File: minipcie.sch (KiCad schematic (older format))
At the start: 1 part

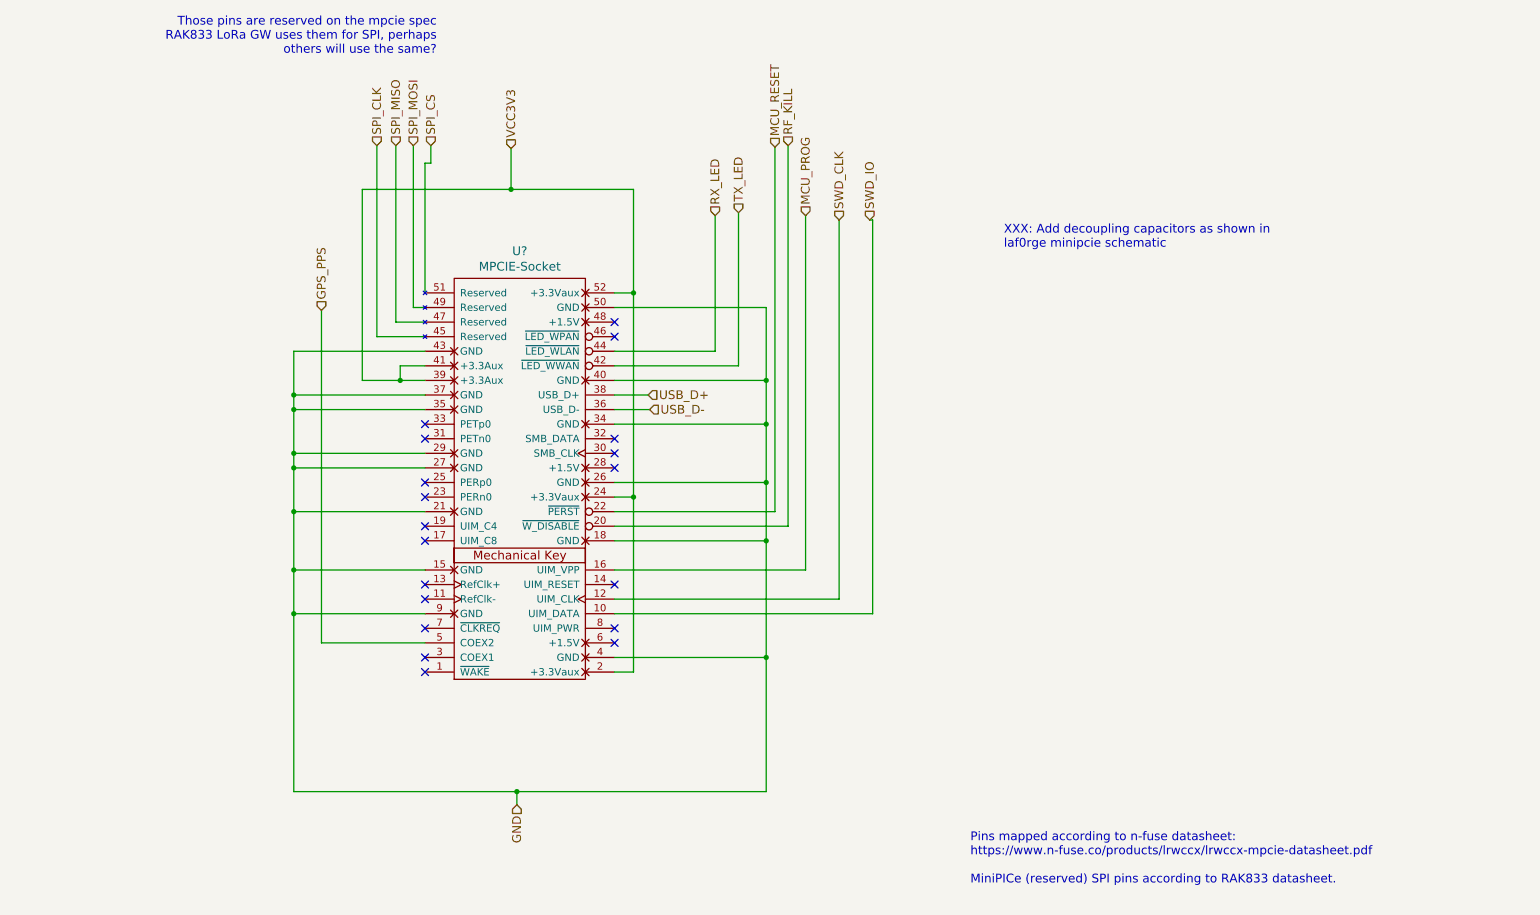
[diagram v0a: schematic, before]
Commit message: Add all POE logic with the si3404, schematic almost finished.
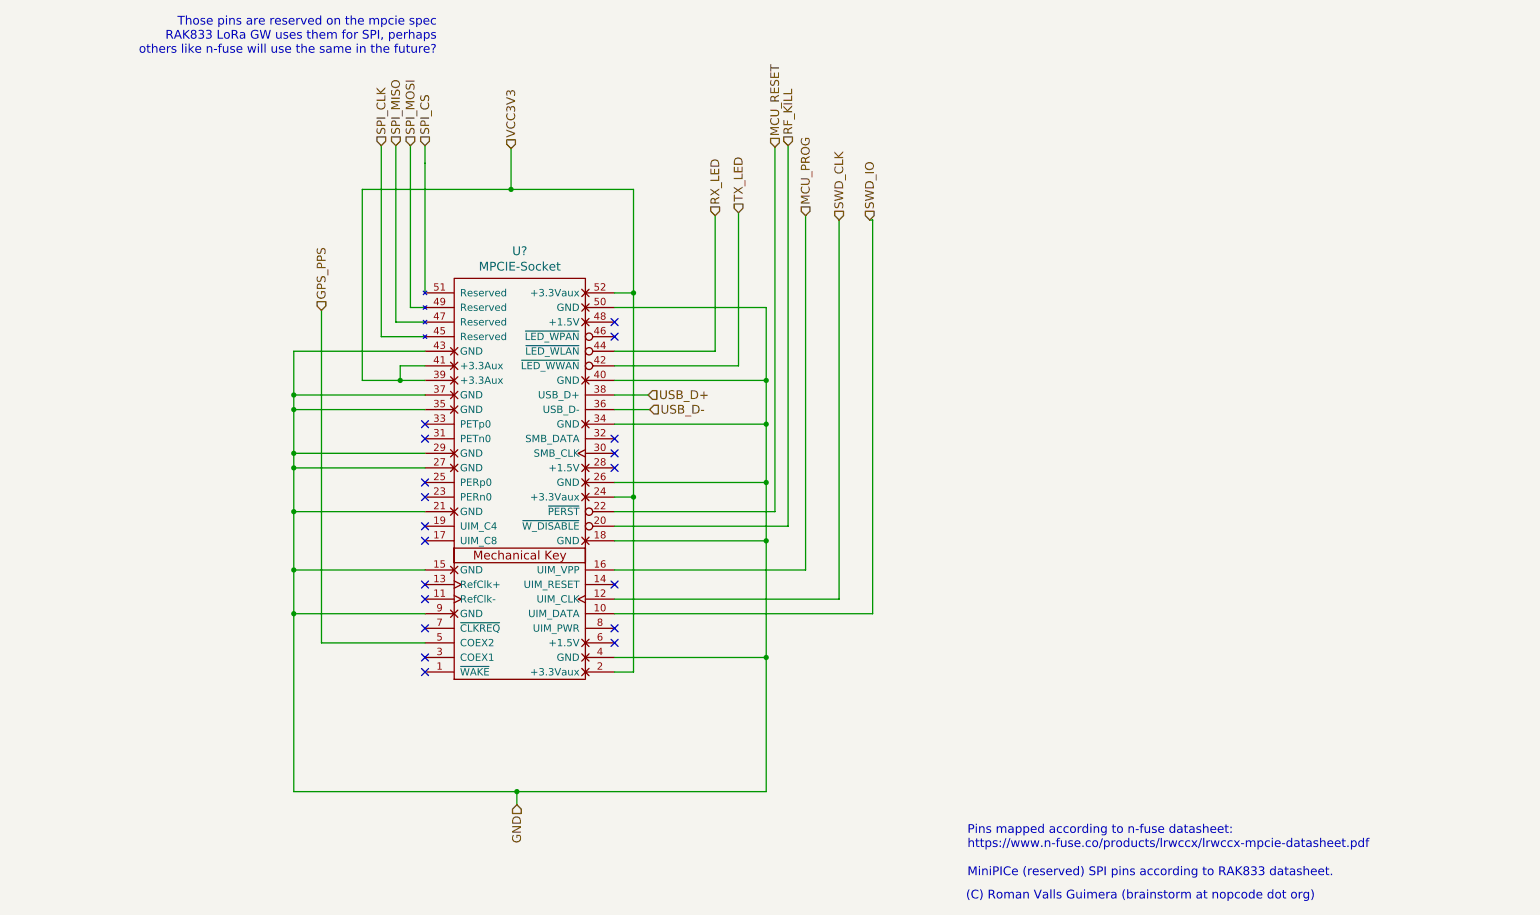
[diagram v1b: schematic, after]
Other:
- note added: "(C) Roman Valls Guimera (brainstorm at nopcode dot org)"
- note added: "Those pins are reserved on the mpcie spec\nRAK833 LoRa GW uses them for SPI, perhaps\nothers like n-fuse will use the same in the future?"
- note removed: "Those pins are reserved on the mpcie spec\nRAK833 LoRa GW uses them for SPI, perhaps\nothers will use the same?"
- note removed: "XXX: Add decoupling capacitors as shown in\nlaf0rge minipcie schematic"
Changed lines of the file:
@@
 LIBS:mpcie
 LIBS:si3406
+LIBS:si3404
+LIBS:SI-52003-F
+LIBS:ap2112
 LIBS:minipcie-eth-cache
 EELAYER 26 0
@@
 $Descr A4 11693 8268
 encoding utf-8
-Sheet 5 4
+Sheet 4 4
 Title ""
 Date ""
@@
 NoConn ~ 4590 3130
 NoConn ~ 4590 3230
-Text Notes 7030 6990 0    60   ~ 0
+Text Notes 7010 6940 0    60   ~ 0
 Pins mapped according to n-fuse datasheet: \nhttps://www.n-fuse.co/products/lrwccx/lrwccx-mpcie-datasheet.pdf\n\nMiniPICe (reserved) SPI pins according to RAK833 datasheet.
 Text HLabel 5440 2380 1    60   Input ~ 0
@@
 Text HLabel 2580 3050 1    60   Input ~ 0
 GPS_PPS
-Text HLabel 2960 1920 1    60   Input ~ 0
+Text HLabel 2990 1920 1    60   Input ~ 0
 SPI_CLK
 Text HLabel 3090 1920 1    60   Input ~ 0
 SPI_MISO
-Text HLabel 3210 1920 1    60   Input ~ 0
+Text HLabel 3190 1920 1    60   Input ~ 0
 SPI_MOSI
-Text HLabel 3330 1920 1    60   Input ~ 0
+Text HLabel 3290 1920 1    60   Input ~ 0
 SPI_CS
 Wire Wire Line
@@
 	4590 3030 5630 3030
 Wire Wire Line
-	5630 3030 5630 6350
+	5630 3030 5630 3530
+Wire Wire Line
+	5630 3530 5630 3830
+Wire Wire Line
+	5630 3830 5630 4230
+Wire Wire Line
+	5630 4230 5630 4630
+Wire Wire Line
+	5630 4630 5630 5430
+Wire Wire Line
+	5630 5430 5630 6350
 Wire Wire Line
 	5630 5430 4590 5430
@@
 	3290 3330 2390 3330
 Wire Wire Line
-	2390 3330 2390 6350
+	2390 3330 2390 3630
+Wire Wire Line
+	2390 3630 2390 3730
+Wire Wire Line
+	2390 3730 2390 4030
+Wire Wire Line
+	2390 4030 2390 4130
+Wire Wire Line
+	2390 4130 2390 4430
+Wire Wire Line
+	2390 4430 2390 4830
+Wire Wire Line
+	2390 4830 2390 5130
+Wire Wire Line
+	2390 5130 2390 6350
 Wire Wire Line
 	2390 5130 3290 5130
@@
 Connection ~ 2390 4830
 Wire Wire Line
-	2390 6350 5630 6350
+	2390 6350 3920 6350
+Wire Wire Line
+	3920 6350 5630 6350
 Connection ~ 5630 5430
 Connection ~ 2390 5130
@@
 Connection ~ 3920 6350
 Wire Wire Line
-	2860 3530 3290 3530
+	2860 3530 3120 3530
+Wire Wire Line
+	3120 3530 3290 3530
 Wire Wire Line
 	2860 3530 2860 2220
 Wire Wire Line
-	2860 2220 4720 2220
-Wire Wire Line
-	4720 2220 4720 5530
+	2860 2220 3880 2220
+Wire Wire Line
+	3880 2220 4720 2220
+Wire Wire Line
+	4720 2220 4720 2930
+Wire Wire Line
+	4720 2930 4720 4330
+Wire Wire Line
+	4720 4330 4720 5530
 Wire Wire Line
 	4720 2930 4590 2930
@@
 	3290 2930 3290 2040
 Wire Wire Line
-	3290 2040 3330 2040
-Wire Wire Line
-	3330 2040 3330 1920
-Wire Wire Line
-	3290 3030 3210 3030
-Wire Wire Line
-	3210 3030 3210 1920
+	3290 2040 3290 2040
+Wire Wire Line
+	3290 2040 3290 1920
+Wire Wire Line
+	3290 3030 3190 3030
+Wire Wire Line
+	3190 3030 3190 1920
 Wire Wire Line
 	3290 3130 3090 3130
@@
 	3090 3130 3090 1920
 Wire Wire Line
-	3290 3230 2960 3230
-Wire Wire Line
-	2960 3230 2960 1920
+	3290 3230 2990 3230
+Wire Wire Line
+	2990 3230 2990 1920
 Text Notes 3370 1300 2    60   ~ 0
-Those pins are reserved on the mpcie spec\nRAK833 LoRa GW uses them for SPI, perhaps\nothers will use the same?
-Text Notes 7260 2630 0    60   ~ 0
-XXX: Add decoupling capacitors as shown in\nlaf0rge minipcie schematic
+Those pins are reserved on the mpcie spec\nRAK833 LoRa GW uses them for SPI, perhaps\nothers like n-fuse will use the same in the future?
+Text Notes 7000 7100 0    60   ~ 0
+(C) Roman Valls Guimera (brainstorm at nopcode dot org)
 $EndSCHEMATC

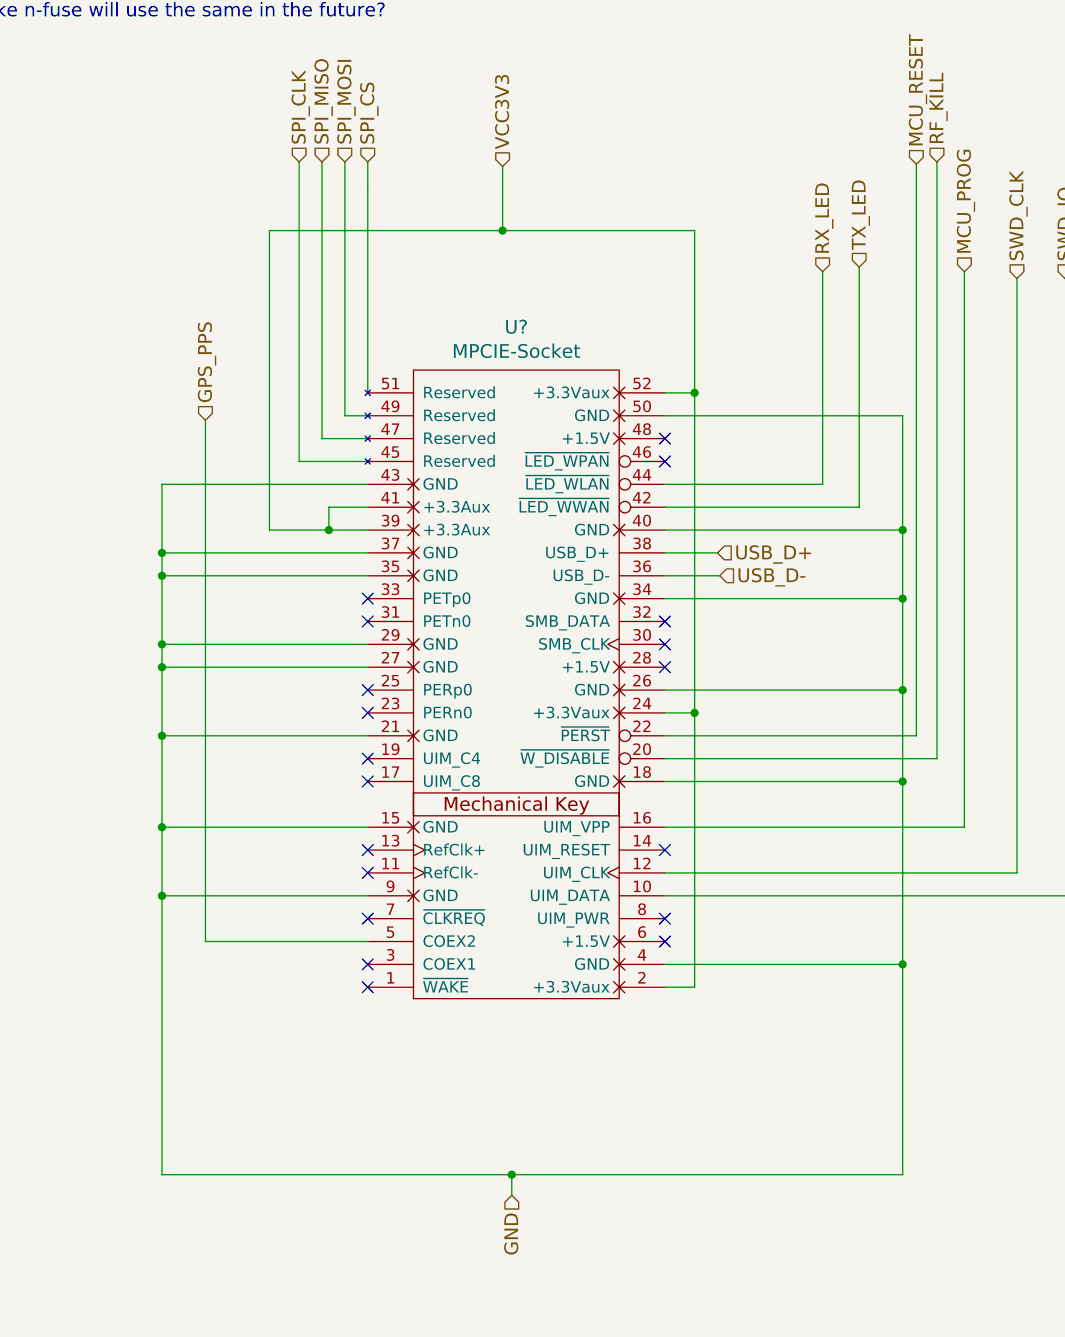
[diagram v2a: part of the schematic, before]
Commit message: Rearrange components, validate package sizes, think about power plane placement since the ref design is 4 layers... can I add snubbers and other filtering and avoid 4-layer design?
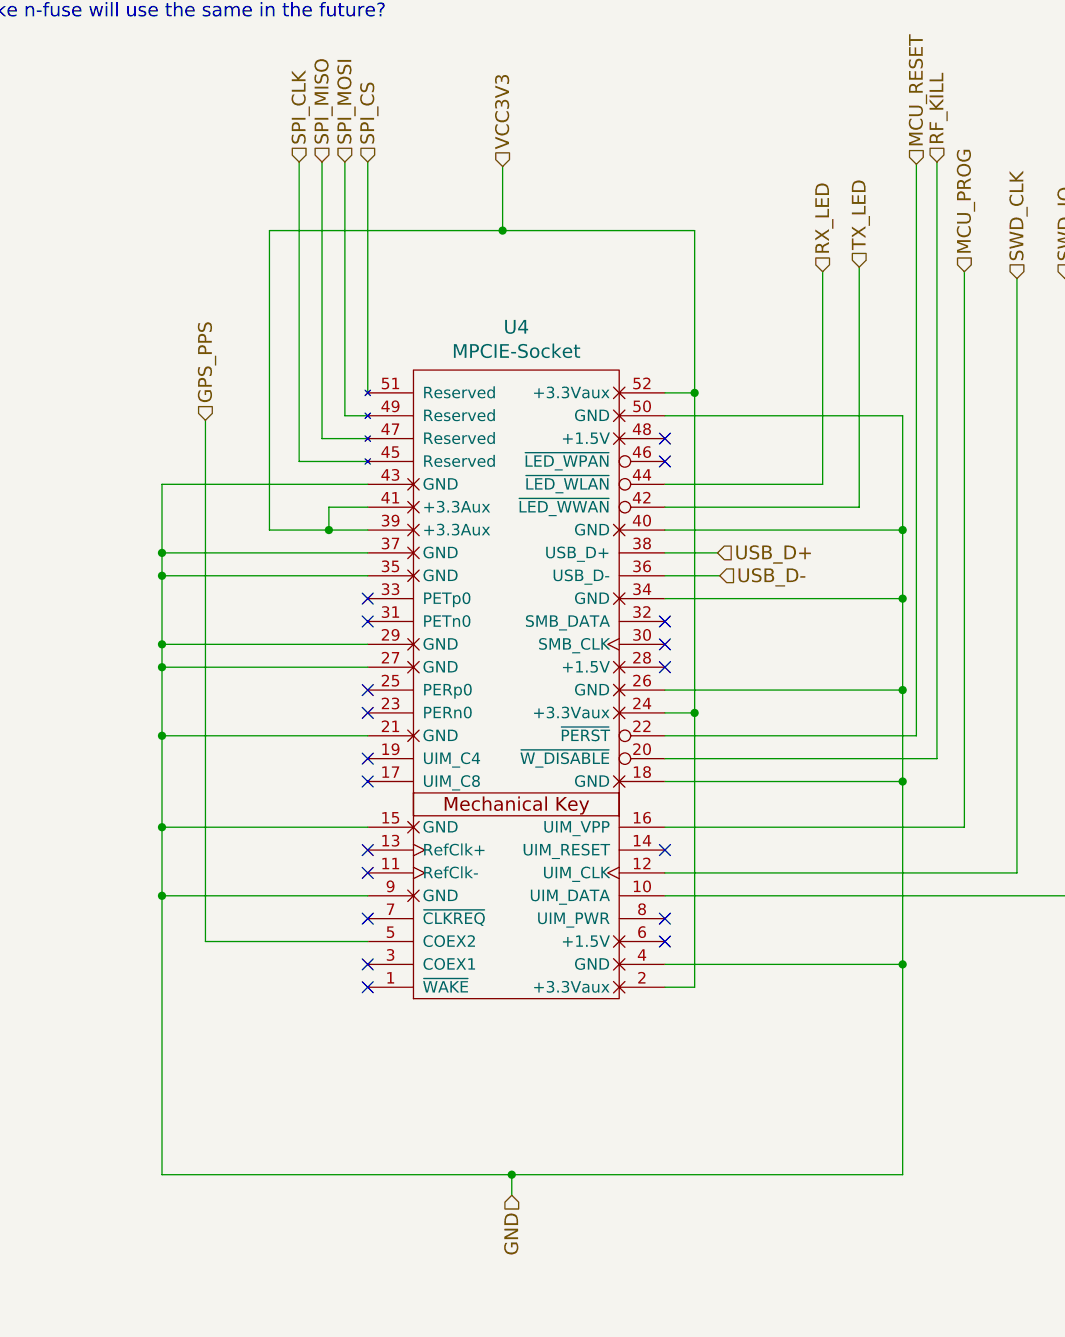
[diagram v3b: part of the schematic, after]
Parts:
- U4: renamed from U?; footprint (none) -> mpcie:mpcie-socket
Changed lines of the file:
@@
 $EndDescr
 $Comp
-L MPCIE-Socket U?
+L MPCIE-Socket U4
 U 1 1 5BB36495
 P 3940 4080
-F 0 "U?" H 3940 5517 60  0000 C CNN
+F 0 "U4" H 3940 5517 60  0000 C CNN
 F 1 "MPCIE-Socket" H 3940 5411 60  0000 C CNN
-F 2 "" H 4040 3080 60  0000 C CNN
+F 2 "mpcie:mpcie-socket" H 4040 3080 60  0001 C CNN
 F 3 "" H 4040 3080 60  0000 C CNN
 	1    3940 4080
@@
 	4590 3030 5630 3030
 Wire Wire Line
-	5630 3030 5630 3530
-Wire Wire Line
-	5630 3530 5630 3830
-Wire Wire Line
-	5630 3830 5630 4230
-Wire Wire Line
-	5630 4230 5630 4630
-Wire Wire Line
-	5630 4630 5630 5430
-Wire Wire Line
-	5630 5430 5630 6350
+	5630 3030 5630 6350
 Wire Wire Line
 	5630 5430 4590 5430
@@
 	3290 3330 2390 3330
 Wire Wire Line
-	2390 3330 2390 3630
-Wire Wire Line
-	2390 3630 2390 3730
-Wire Wire Line
-	2390 3730 2390 4030
-Wire Wire Line
-	2390 4030 2390 4130
-Wire Wire Line
-	2390 4130 2390 4430
-Wire Wire Line
-	2390 4430 2390 4830
-Wire Wire Line
-	2390 4830 2390 5130
-Wire Wire Line
-	2390 5130 2390 6350
+	2390 3330 2390 6350
 Wire Wire Line
 	2390 5130 3290 5130
@@
 Connection ~ 2390 4830
 Wire Wire Line
-	2390 6350 3920 6350
-Wire Wire Line
-	3920 6350 5630 6350
+	2390 6350 5630 6350
 Connection ~ 5630 5430
 Connection ~ 2390 5130
@@
 Connection ~ 3920 6350
 Wire Wire Line
-	2860 3530 3120 3530
-Wire Wire Line
-	3120 3530 3290 3530
+	2860 3530 3290 3530
 Wire Wire Line
 	2860 3530 2860 2220
 Wire Wire Line
-	2860 2220 3880 2220
+	2860 2220 4720 2220
 Wire Wire Line
-	3880 2220 4720 2220
-Wire Wire Line
-	4720 2220 4720 2930
-Wire Wire Line
-	4720 2930 4720 4330
-Wire Wire Line
-	4720 4330 4720 5530
+	4720 2220 4720 5530
 Wire Wire Line
 	4720 2930 4590 2930
@@
 	2580 5330 2580 3050
 Wire Wire Line
-	3290 2930 3290 2040
-Wire Wire Line
-	3290 2040 3290 2040
-Wire Wire Line
-	3290 2040 3290 1920
+	3290 1920 3290 2930
 Wire Wire Line
 	3290 3030 3190 3030

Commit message: Migrate to KiCad 5.1 :)
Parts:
- U4: symbol MPCIE-Socket -> mpcie:MPCIE-Socket
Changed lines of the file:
@@
-EESchema Schematic File Version 3
-LIBS:power
-LIBS:device
-LIBS:transistors
-LIBS:conn
-LIBS:linear
-LIBS:regul
-LIBS:74xx
-LIBS:cmos4000
-LIBS:adc-dac
-LIBS:memory
-LIBS:xilinx
-LIBS:microcontrollers
-LIBS:dsp
-LIBS:microchip
-LIBS:analog_switches
-LIBS:motorola
-LIBS:texas
-LIBS:intel
-LIBS:audio
-LIBS:interface
-LIBS:digital-audio
-LIBS:philips
-LIBS:display
-LIBS:cypress
-LIBS:siliconi
-LIBS:opto
-LIBS:atmel
-LIBS:contrib
-LIBS:valves
-LIBS:win
-LIBS:freetronics_schematic
-LIBS:mpcie
-LIBS:si3406
-LIBS:si3404
-LIBS:SI-52003-F
-LIBS:ap2112
+EESchema Schematic File Version 4
 LIBS:minipcie-eth-cache
-EELAYER 26 0
+EELAYER 29 0
 EELAYER END
 $Descr A4 11693 8268
 encoding utf-8
-Sheet 3 4
+Sheet 3 3
 Title ""
 Date ""
@@
 $EndDescr
 $Comp
-L MPCIE-Socket U4
+L mpcie:MPCIE-Socket U4
 U 1 1 5BB36495
 P 3940 4080
